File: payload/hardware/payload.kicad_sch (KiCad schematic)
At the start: 0 parts

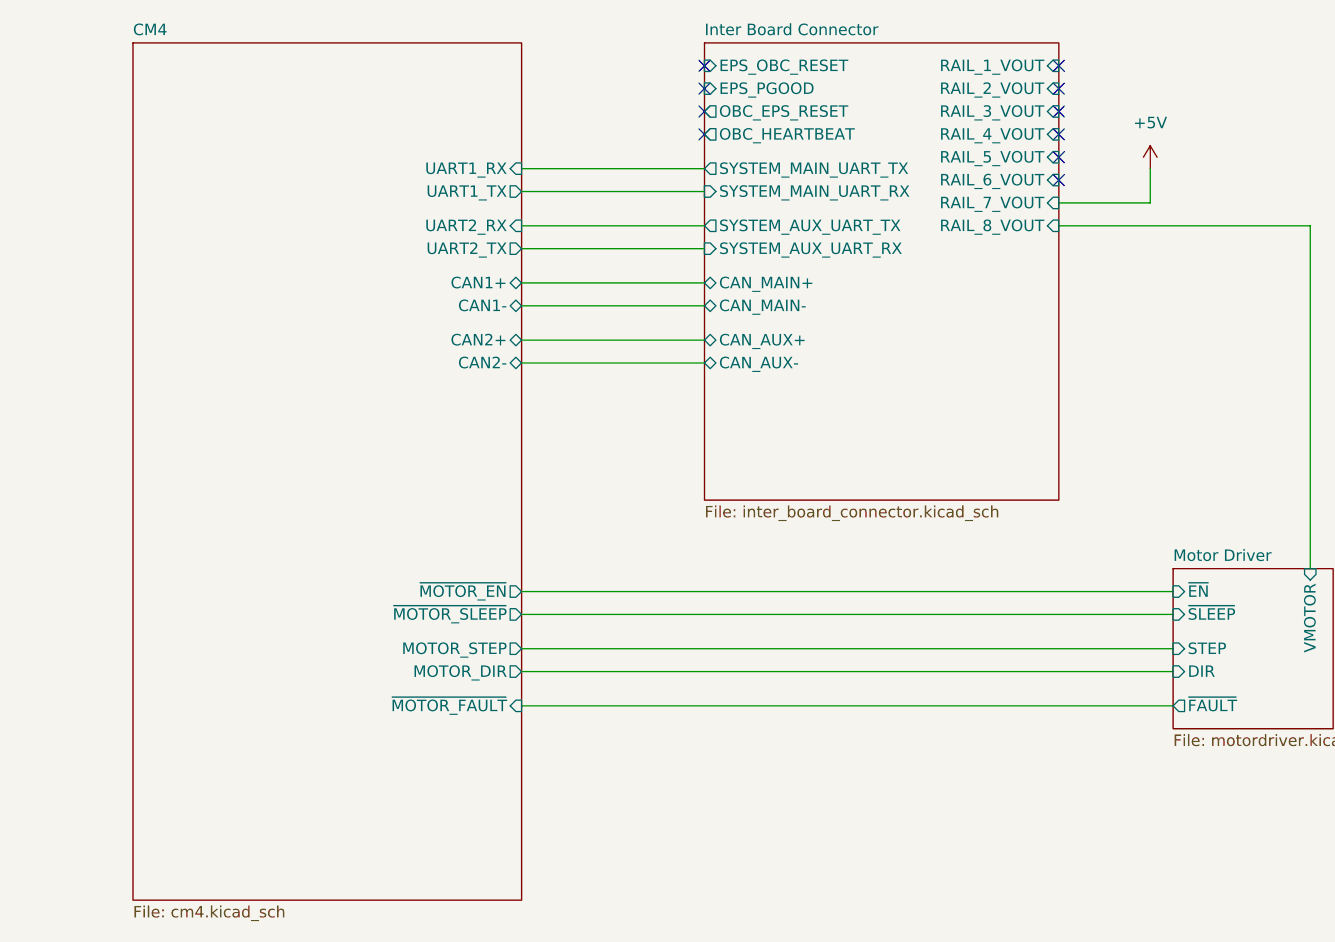
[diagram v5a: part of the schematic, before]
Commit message: add decoupling caps, fix USB skew, add Jax's name
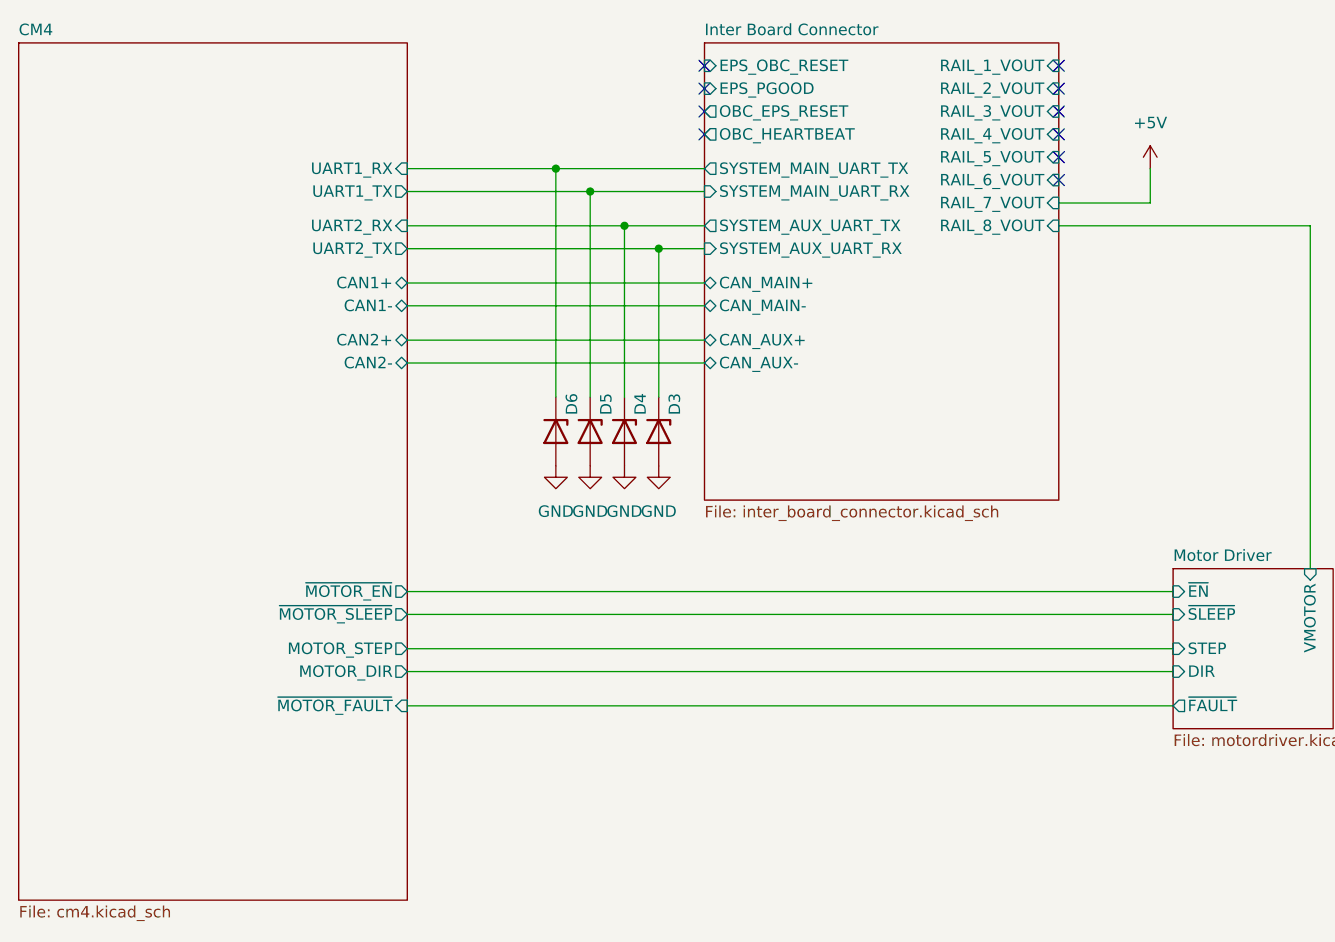
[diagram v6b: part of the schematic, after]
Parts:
- added D3, D4, D5, D6: D_Zener, Diode_SMD:D_SOD-323, symbol Device:D_Zener
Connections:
- net CM4/UART1_RX: now also D6.1 (K)
- net CM4/UART1_TX: now also D5.1 (K)
- net CM4/UART2_RX: now also D4.1 (K)
- net CM4/UART2_TX: now also D3.1 (K)
- new net GND: D3.2 (A), D4.2 (A), D5.2 (A), D6.2 (A)

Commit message: ERC fixes, nits, NC
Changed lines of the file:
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@@
 	(paper "A4")
+	(junction
+		(at 152.4 59.69)
+		(diameter 0)
+		(color 0 0 0 0)
+	)
 	(junction
 		(at 92.71 55.88)
@@
 		(color 0 0 0 0)
 	)
+	(junction
+		(at 152.4 57.15)
+		(diameter 0)
+		(color 0 0 0 0)
+	)
 	(no_connect
 		(at 144.78 41.91)
@@
 	(wire
 		(pts
-			(xy 172.72 59.69) (xy 144.78 59.69)
-		)
-		(stroke
-			(width 0)
-			(type default)
-		)
-	)
-	(wire
-		(pts
-			(xy 154.94 57.15) (xy 154.94 53.34)
+			(xy 172.72 59.69) (xy 152.4 59.69)
+		)
+		(stroke
+			(width 0)
+			(type default)
+		)
+	)
+	(wire
+		(pts
+			(xy 160.02 57.15) (xy 160.02 53.34)
 		)
 		(stroke
@@
 	(wire
 		(pts
+			(xy 152.4 59.69) (xy 152.4 67.31)
+		)
+		(stroke
+			(width 0)
+			(type default)
+		)
+	)
+	(wire
+		(pts
 			(xy 72.39 109.22) (xy 157.48 109.22)
 		)
@@
 	(wire
 		(pts
-			(xy 144.78 57.15) (xy 154.94 57.15)
+			(xy 152.4 57.15) (xy 160.02 57.15)
+		)
+		(stroke
+			(width 0)
+			(type default)
+		)
+	)
+	(wire
+		(pts
+			(xy 144.78 57.15) (xy 152.4 57.15)
 		)
 		(stroke
@@
 	(wire
 		(pts
+			(xy 152.4 49.53) (xy 152.4 57.15)
+		)
+		(stroke
+			(width 0)
+			(type default)
+		)
+	)
+	(wire
+		(pts
 			(xy 72.39 74.93) (xy 105.41 74.93)
+		)
+		(stroke
+			(width 0)
+			(type default)
+		)
+	)
+	(wire
+		(pts
+			(xy 152.4 59.69) (xy 144.78 59.69)
 		)
 		(stroke
@@
 	(symbol
 		(lib_id "power:+5V")
-		(at 154.94 53.34 0)
+		(at 160.02 53.34 0)
 		(unit 1)
 		(body_style 1)
@@
 		(fields_autoplaced yes)
 		(property "Reference" "#PWR040"
-			(at 154.94 57.15 0)
+			(at 160.02 57.15 0)
 			(hide yes)
 			(show_name no)
@@
 		)
 		(property "Value" "+5V"
-			(at 154.94 48.26 0)
+			(at 160.02 48.26 0)
 			(show_name no)
 			(do_not_autoplace no)
@@
 		)
 		(property "Footprint" ""
-			(at 154.94 53.34 0)
+			(at 160.02 53.34 0)
 			(hide yes)
 			(show_name no)
@@
 		)
 		(property "Datasheet" ""
-			(at 154.94 53.34 0)
+			(at 160.02 53.34 0)
 			(hide yes)
 			(show_name no)
@@
 		)
 		(property "Description" "Power symbol creates a global label with name \"+5V\""
-			(at 154.94 53.34 0)
+			(at 160.02 53.34 0)
 			(hide yes)
 			(show_name no)
@@
 				(path "/6c55f0ca-d6e4-4a04-9323-ecf7d8843170"
 					(reference "#PWR040")
+					(unit 1)
+				)
+			)
+		)
+	)
+	(symbol
+		(lib_id "power:PWR_FLAG")
+		(at 152.4 49.53 0)
+		(unit 1)
+		(body_style 1)
+		(exclude_from_sim no)
+		(in_bom yes)
+		(on_board yes)
+		(in_pos_files yes)
+		(dnp no)
+		(fields_autoplaced yes)
+		(property "Reference" "#FLG01"
+			(at 152.4 47.625 0)
+			(hide yes)
+			(show_name no)
+			(do_not_autoplace no)
+			(effects
+				(font
+					(size 1.27 1.27)
+				)
+			)
+		)
+		(property "Value" "PWR_FLAG"
+			(at 152.4 44.45 0)
+			(show_name no)
+			(do_not_autoplace no)
+			(effects
+				(font
+					(size 1.27 1.27)
+				)
+			)
+		)
+		(property "Footprint" ""
+			(at 152.4 49.53 0)
+			(hide yes)
+			(show_name no)
+			(do_not_autoplace no)
+			(effects
+				(font
+					(size 1.27 1.27)
+				)
+			)
+		)
+		(property "Datasheet" ""
+			(at 152.4 49.53 0)
+			(hide yes)
+			(show_name no)
+			(do_not_autoplace no)
+			(effects
+				(font
+					(size 1.27 1.27)
+				)
+			)
+		)
+		(property "Description" "Special symbol for telling ERC where power comes from"
+			(at 152.4 49.53 0)
+			(hide yes)
+			(show_name no)
+			(do_not_autoplace no)
+			(effects
+				(font
+					(size 1.27 1.27)
+				)
+			)
+		)
+		(pin "1"
+		)
+		(instances
+			(project "payload"
+				(path "/6c55f0ca-d6e4-4a04-9323-ecf7d8843170"
+					(reference "#FLG01")
 					(unit 1)
 				)
@@
 					(unit 1)
 				)
+			)
+		)
+	)
+	(symbol
+		(lib_id "power:PWR_FLAG")
+		(at 152.4 67.31 180)
+		(unit 1)
+		(body_style 1)
+		(exclude_from_sim no)
+		(in_bom yes)
+		(on_board yes)
+		(in_pos_files yes)
+		(dnp no)
+		(fields_autoplaced yes)
+		(property "Reference" "#FLG02"
+			(at 152.4 69.215 0)
+			(hide yes)
+			(show_name no)
+			(do_not_autoplace no)
+			(effects
+				(font
+					(size 1.27 1.27)
+				)
+			)
+		)
+		(property "Value" "PWR_FLAG"
+			(at 152.4 72.39 0)
+			(show_name no)
+			(do_not_autoplace no)
+			(effects
+				(font
+					(size 1.27 1.27)
+				)
+			)
+		)
+		(property "Footprint" ""
+			(at 152.4 67.31 0)
+			(hide yes)
+			(show_name no)
+			(do_not_autoplace no)
+			(effects
+				(font
+					(size 1.27 1.27)
+				)
+			)
+		)
+		(property "Datasheet" ""
+			(at 152.4 67.31 0)
+			(hide yes)
+			(show_name no)
+			(do_not_autoplace no)
+			(effects
+				(font
+					(size 1.27 1.27)
+				)
+			)
+		)
+		(property "Description" "Special symbol for telling ERC where power comes from"
+			(at 152.4 67.31 0)
+			(hide yes)
+			(show_name no)
+			(do_not_autoplace no)
+			(effects
+				(font
+					(size 1.27 1.27)
+				)
+			)
+		)
+		(pin "1"
+		)
+		(instances
+			(project "payload"
+				(path "/6c55f0ca-d6e4-4a04-9323-ecf7d8843170"
+					(reference "#FLG02")
+					(unit 1)
+				)

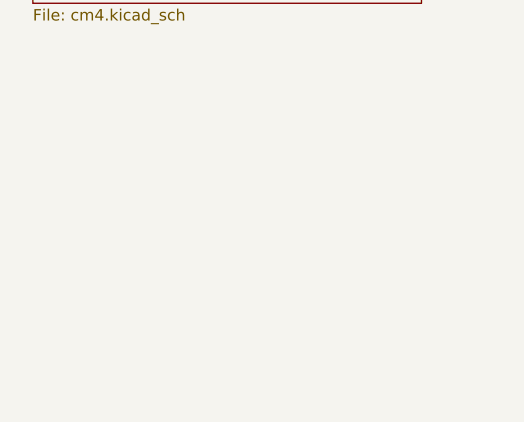
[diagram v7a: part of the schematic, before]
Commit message: mounting holes
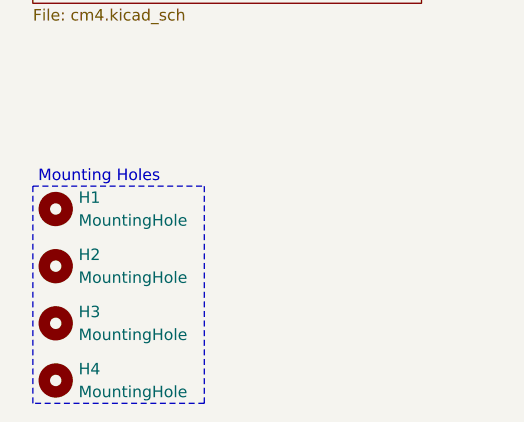
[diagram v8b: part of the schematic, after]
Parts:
- added H1, H2, H3, H4: MountingHole, MountingHole:MountingHole_3.2mm_M3, symbol Mechanical:MountingHole
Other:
- note added: "Mounting Holes"
